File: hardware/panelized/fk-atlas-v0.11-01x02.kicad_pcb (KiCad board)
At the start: 4 copper layers, 106.4 x 181.6 mm, 340 parts, among them J1 CONN_02x05_SWD, J10 CONN_01x04, J2 MICRO-USB-VERT-TOP, J201 CONN_01X02, J3 CONN_01x02, J301 CONN_01X02, J4 CONN_01x03_SERIAL, J401 CONN_01X02, J5 CONN_01x05, J501 CONN_01X02, J6 CONN_01x04, J601 CONN_01X02, J7 CONN_01x05, J8 CONN_01x02, J9 MICRO-USB-HORIZ-BOTTOM, M1 MOUNT_HOLE, M2 MOUNT_HOLE, M3 MOUNT_HOLE, M4 MOUNT_HOLE, M5 FIDUCIAL, M6 FIDUCIAL, M7 FIDUCIAL, P2 ATLAS_EC_PROBE, P3 ATLAS_RTD_PROBE, P4 ATLAS_PH_PROBE, P5 ATLAS_DO_PROBE, P6 ATLAS_ORP_PROBE, Q4 2N7002LT1G, SW1 SPNO, U1 S25FL116K0XMFI041, U2 ATSAMD21G18A-AU, U201 ADM3260, U202 ATLAS_EC, U3 MCP1700T-3302E/MB, U301 ADM3260, U302 ATLAS_RTD, U4 TPS2052B, U401 ADM3260, U402 ATLAS_PH, U5 SK6812, U501 ADM3260, U502 ATLAS_DO, U601 ADM3260, U602 ATLAS_ORP, Y1 FC-135

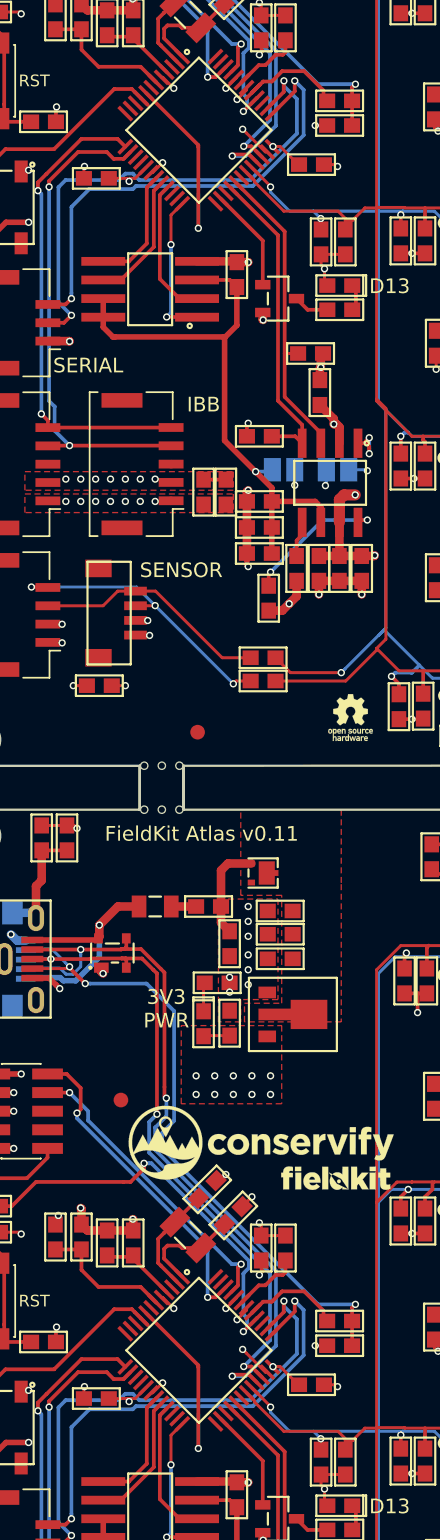
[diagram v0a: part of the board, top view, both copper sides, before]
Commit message: Cleaned up old gerber files and regenerated panelized gerbers and original file after fab found an unconnected track (A2, wasn't used for anything)
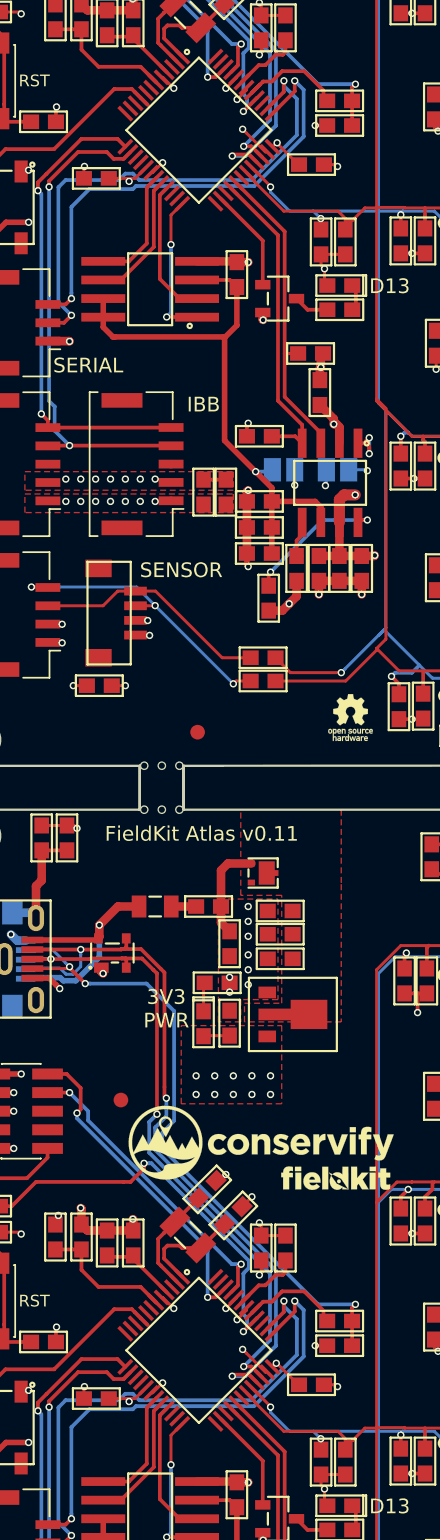
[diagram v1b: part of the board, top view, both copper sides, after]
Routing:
- net /A2: track 26.1 -> 0.00 mm, vias 2 -> 0
